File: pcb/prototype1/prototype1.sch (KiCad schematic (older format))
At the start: 87 parts, among them P1 AAA1 HOT, P2 AAA1 GND, P3 AAA2 GND, P4 AAA2 HOT, P5 USB_B, SW1 SPST, SW2 Button, SW3 Button, SW4 Button, SW5 Button, U1 STM32F410R8/B, U10 AT25_EEPROM, U2 LD1117S33CTR, U3 TPS61021, U4 L3GD20HTR, U5 LIS331HH, U6 LIS331HH, U7 TLC5926, U8 TLC5926, U9 TLC5926

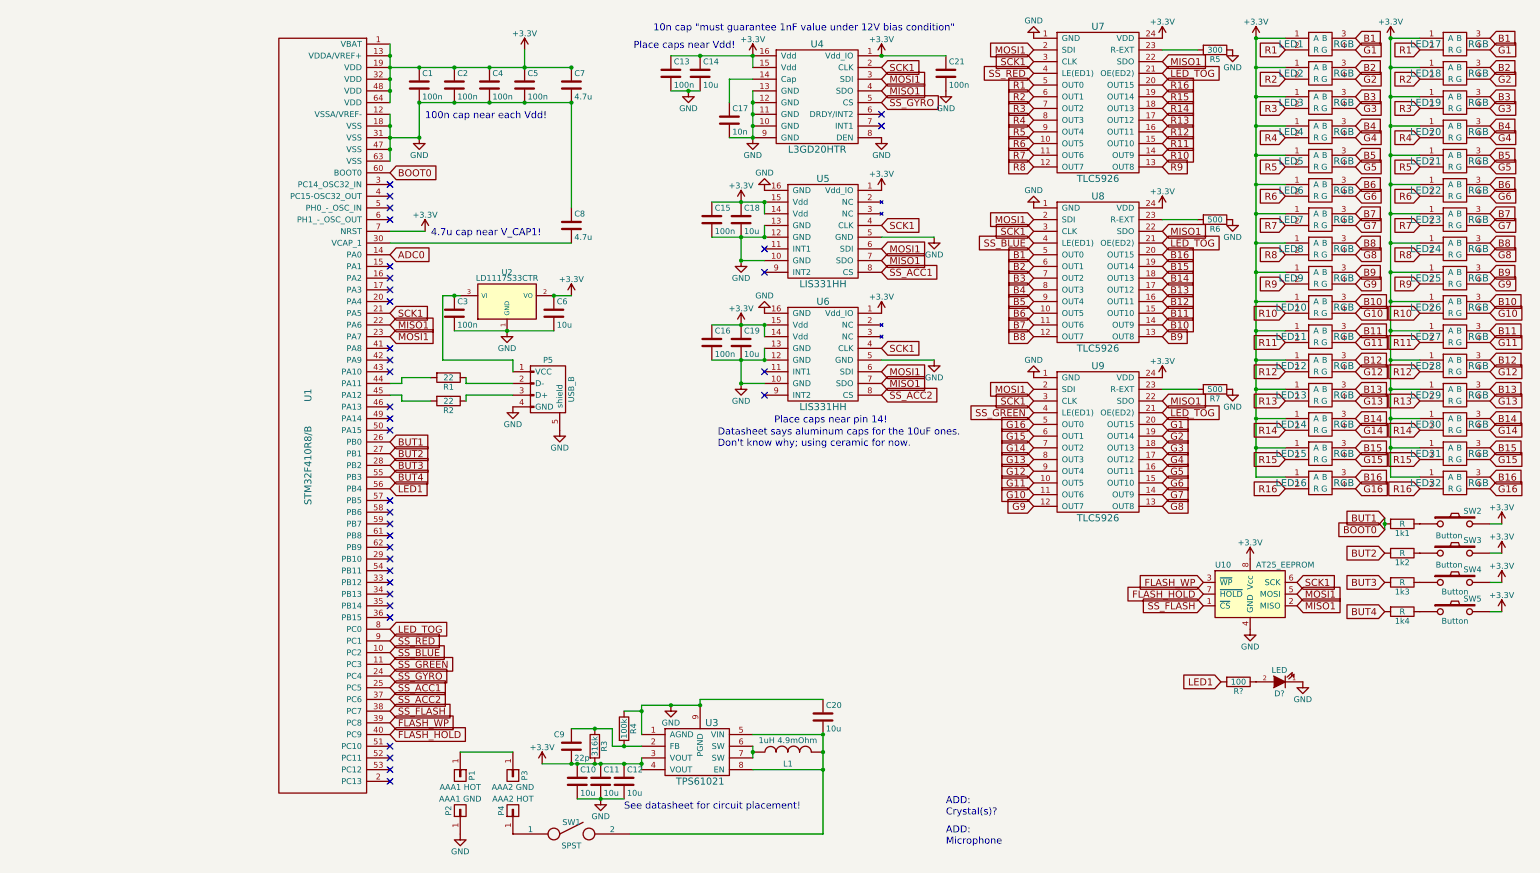
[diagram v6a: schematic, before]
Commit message: Switch to stm32f401
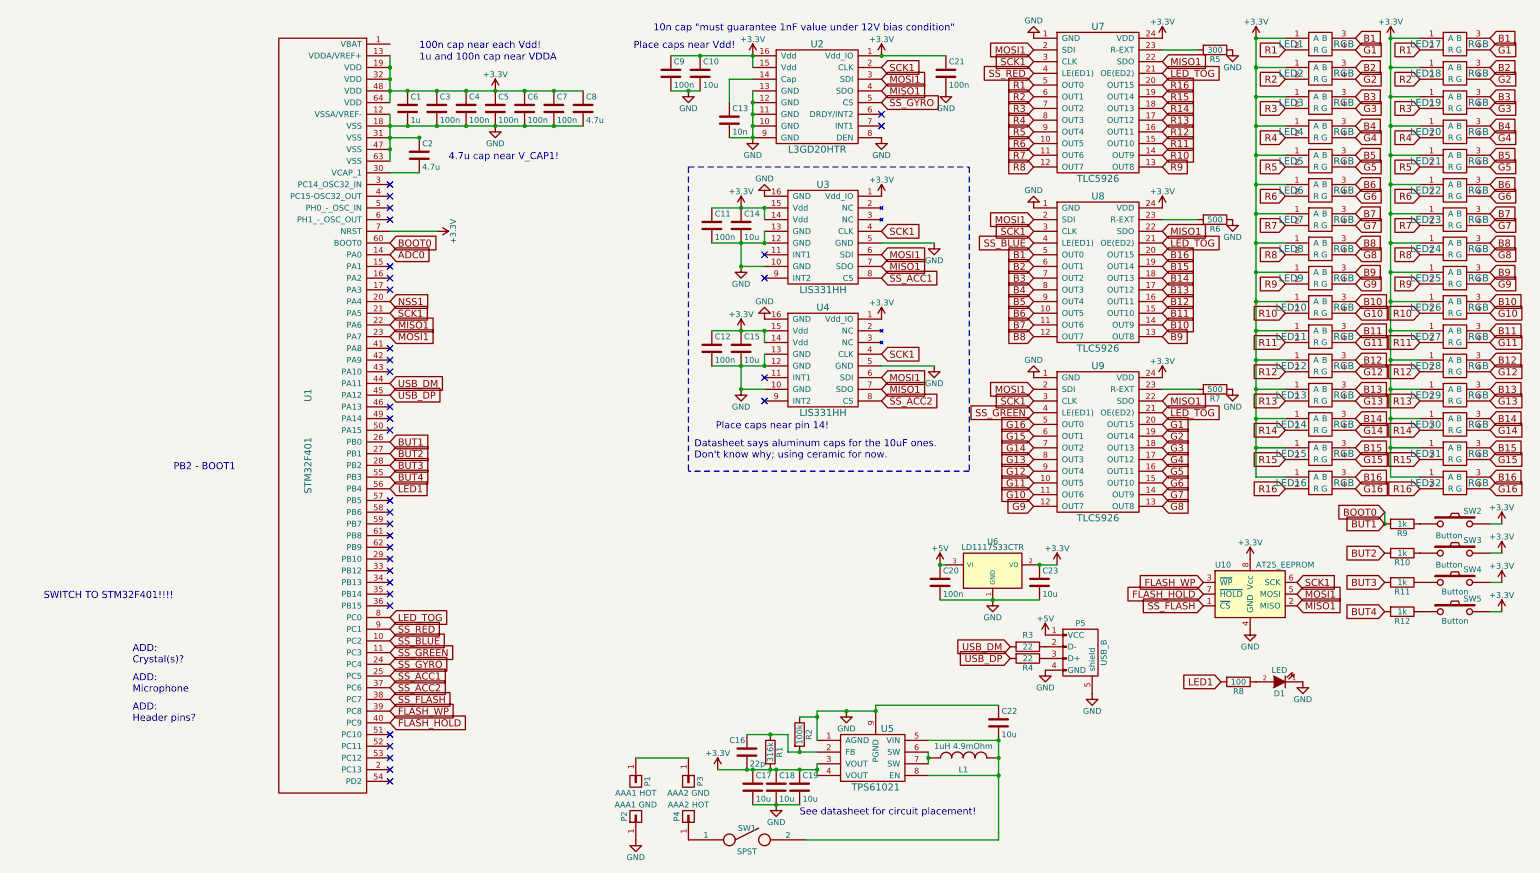
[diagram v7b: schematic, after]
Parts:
- removed 1k2, 1k3, 1k4: R, Resistors_SMD:R_0805_HandSoldering, symbol R
- removed U1: STM32F410R8/B, spin:STM32F410-LQFP64, symbol STM32F410R8/B
- added C1: 1u, Capacitors_SMD:C_0805_HandSoldering, symbol C
- added C3: 100n, Capacitors_SMD:C_0603_HandSoldering, symbol C
- added R10, R11, R12: 1k, Resistors_SMD:R_0805_HandSoldering, symbol R
- added U1: STM32F401, Housings_QFP:TQFP-64_10x10mm_Pitch0.5mm, symbol STM32F401
- R9: renamed from 1k1; value R -> 1k
- gave numbers to parts that had none: 2
- renumbered C14 to C10, C15 to C11, C16 to C12, C17 to C13, C18 to C14, C19 to C15, C9 to C16, C10 to C17, C11 to C18, C12 to C19, C8 to C2, C3 to C20, C20 to C22, C6 to C23, C1 to C4, C2 to C5, C4 to C6, C5 to C7, C7 to C8, C13 to C9, R3 to R1, R4 to R2, R1 to R3, R2 to R4, U4 to U2, U5 to U3, U6 to U4, U3 to U5, U2 to U6
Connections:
- net +3V3: now also C1.1, C3.1, U1.13 (VDDA/VREF+), U1.19 (VDD), U1.32 (VDD), U1.48 (VDD), U1.64 (VDD), U1.7 (NRST)
- net ADC0: now also U1.14 (PA0)
- net BOOT0: now also U1.26 (PB0), U1.60 (BOOT0)
- net BUT2: now also R10.2, U1.27 (PB1)
- net BUT3: now also R11.2, U1.28 (PB2)
- net BUT4: now also R12.2, U1.55 (PB3)
- net FLASH_HOLD: now also U1.40 (PC9)
- net FLASH_WP: now also U1.39 (PC8)
- net GND: now also C1.2, C3.2, U1.12 (VSSA/VREF-), U1.18 (VSS), U1.31 (VSS), U1.47 (VSS), U1.63 (VSS)
- net LED1: now also U1.56 (PB4)
- net LED_TOG: now also U1.8 (PC0)
- net MISO1: now also U1.22 (PA6)
- net MOSI1: now also U1.23 (PA7)
- net SCK1: now also U1.21 (PA5)
- net SS_ACC1: now also U1.25 (PC5)
- net SS_ACC2: now also U1.37 (PC6)
- net SS_BLUE: now also U1.10 (PC2)
- net SS_FLASH: now also U1.38 (PC7)
- net SS_GREEN: now also U1.11 (PC3)
- net SS_GYRO: now also U1.24 (PC4)
- net SS_RED: now also U1.9 (PC1)
- net +5V: now reaches C20.1, P5.1 (VCC), U6.3 (VI)
- net USB_DM: now reaches R3.2
- net USB_DM: now also U1.44 (PA11)
- net at C2.2: now also U1.30 (VCAP_1)
- net USB_DP: now reaches R4.2
- net USB_DP: now also U1.45 (PA12)
- net at SW3.1: now also R10.1
- net at SW4.1: now also R11.1
- net at SW5.1: now also R12.1
- new net NSS1: U1.20 (PA4)
- no-connect marks 35 -> 34
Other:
- note added: "1u and 100n cap near VDDA"
- note added: "ADD:\nHeader pins?"
- note added: "PB2 - BOOT1"
- note added: "SWITCH TO STM32F401!!!!"
- moved on the sheet: C11, C12, C14, C15, C16, C17, C18, C19, C2, C20, C22, C23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

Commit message: Schematic mostly done
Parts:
- removed R10, R11, R12: 1k, Resistors_SMD:R_0805_HandSoldering, symbol R
- added C5: 10u, Capacitors_SMD:C_0805_HandSoldering, symbol C
- added C7: 100n, Capacitors_SMD:C_0603_HandSoldering, symbol C
- added R4, R5, R6: 10k, Resistors_SMD:R_0805_HandSoldering, symbol R
- added U2: MP34DT01-M, spin:MP34DT01-M, symbol MP34DT01-M
- C10: renamed from C8; footprint Capacitors_SMD:C_0805_HandSoldering -> Capacitors_SMD:C_0603_HandSoldering; manf# VJ0805G475KXYTW1BC -> CC0603KRX5R5BB475
- C2: footprint Capacitors_SMD:C_0805_HandSoldering -> Capacitors_SMD:C_0603_HandSoldering; manf# VJ0805G475KXYTW1BC -> CC0603KRX5R5BB475
- R10: renamed from R7; value 500 -> <=500
- R3: renamed from R9; value 1k -> 10k; manf# AS08J1001ET -> AS08J1002ET
- R8: renamed from R5; value 300 -> <=300
- R9: renamed from R6; value 500 -> <=500
- U3: renamed from U2; footprint spin:L3GD20H -> spin:LGA16
- renumbered C9 to C11, C10 to C12, C11 to C13, C12 to C14, C13 to C15, C14 to C16, C15 to C17, C16 to C18, C17 to C19, C18 to C20, C19 to C21, C21 to C22, C22 to C23, C20 to C24, C23 to C25, C5 to C6, C6 to C8, C7 to C9, R3 to R11, R4 to R12, R8 to R7, U6 to U11, U3 to U4, U4 to U5, U5 to U6
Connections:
- net +3V3: now also R3.2, U1.1 (VBAT), C5.1, C7.1, R4.2, R5.2, R6.2, U2.1 (Vdd); no longer SW2.2, SW3.2, SW4.2, SW5.2, U1.7 (NRST)
- net BOOT0: now also R3.1, SW2.1; no longer R3.2
- net BUT2: now also SW3.1, R4.1
- net BUT3: now also SW4.1, R5.1
- net BUT4: now also SW5.1, R6.1
- net GND: now also SW2.2, SW3.2, SW4.2, SW5.2, C5.2, C7.2, U2.2 (LR), U2.5 (GND)
- net MIC_CLK: now reaches U1.29 (PB10)
- net MIC_CLK: now also U2.3 (CLK)
- net OSC_IN: now reaches U1.5 (PH0_-_OSC_IN)
- net MIC_DATA: now reaches U1.51 (PC10)
- net MIC_DATA: now also U2.4 (DOUT)
- net OSC_OUT: now reaches U1.6 (PH1_-_OSC_OUT)
- net +5V: no longer names the net of C24.1, P5.1 (VCC), U11.3 (VI)
- net ADC0: no longer names the net of U1.14 (PA0)
- net NSS1: no longer names the net of U1.20 (PA4)
- no-connect marks 34 -> 33
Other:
- note added: "10n cap "must guarantee 1n value under 12V bias condition""
- note added: "1u and 100n cap near VDDA!"
- note added: "ADD:\nCrystal"
- note added: "Accelerometers"
- note added: "Batteries"
- note added: "Buttons"
- note added: "CHANGE SWITCH / DO FOOTPRINT"
- note added: "Caps near Vdd!"
- note added: "Caps near pin 1!"
- note added: "Caps near pin 14!"
- note added: "Crystal"
- note added: "Datasheet says aluminum 10uF caps.\nDon't know why; using ceramic for now."
- note added: "Flash"
- note added: "Gyroscope"
- note added: "LED Drivers"
- note added: "LEDs"
- note added: "Microphone"
- note added: "Test LED"
- note added: "USB Connection"
- note removed: "10n cap "must guarantee 1nF value under 12V bias condition""
- note removed: "1u and 100n cap near VDDA"
- note removed: "ADD:\nCrystal(s)?"
- note removed: "ADD:\nHeader pins?"
- note removed: "ADD:\nMicrophone"
- note removed: "Datasheet says aluminum caps for the 10uF ones.\nDon't know why; using ceramic for now."
- note removed: "PB2 - BOOT1"
- note removed: "Place caps near Vdd!"
- note removed: "Place caps near pin 14!"
- note removed: "SWITCH TO STM32F401!!!!"
- moved on the sheet: C11, C12, C13, C14, C15, C16, C17, C18, C19, C20, C21, C22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
